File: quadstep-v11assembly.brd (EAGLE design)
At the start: 57.8 x 122.4 mm, 115 parts, among them U1 A4983, U3 A4983, U4 A4983, U5 A4983, X1 MSTBA4, X2 MSTBA4, X3 MSTBA4, X4 MSTBA4

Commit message: Clean-up of the layout.
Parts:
- removed C10, C11, C18, C19, C21, C22, C23, C27, C28, C29, C3, C4, C46, C47, C49: 0.1uF, SparkFun:0402-CAP
- removed C20, C6, C8: 0.22uF, SparkFun:0402-CAP
- removed JP1, JP14, JP15, JP2, JP7, JP8: (no value), SparkFun:SCREWTERMINAL-3.5MM-2_LOCK
- removed LED1, LED3, LED4: green, SparkFun:LED-0603
- removed R1, R18, R19, R2, R4, R5: 0.22, SparkFun:0805
- removed R17, R24, R3: Trimpot, SparkFun:TRIMPOT-3MM
- removed R20, R6, R66: 20k, SparkFun:0402-RES
- removed R21, R28, R7: 330, SparkFun:0402-RES
- removed R31, R32, R33, R37, R38, R39, R40, R45, R46, R47, R48, R8: 10k, SparkFun:0402-RES
- removed SJ14, SJ15, SJ16, SJ17, SJ2, SJ3, SJ4, SJ5, SJ6, SJ7, SJ8, SJ9: SOLDERJUMPERNO, SparkFun:SJ_2S-NO
- removed TP1, TP2, TP3: TEST-POINT3X5, SparkFun:PAD.03X.05
- removed U1, U4, U5: A4983, SparkFun:QFN-28-5MM
- removed X1, X2, X4: MSTBA4, con-phoenix-508:MSTBA4
- moved SJ26 69.1 mm to (23.2, 23.3), turned to 90 degrees
- moved C32 68.8 mm to (21.4, 20.7), turned to 90 degrees
- moved R61 65.0 mm to (30.4, 26.7), turned to 90 degrees
- moved C30 60.3 mm to (27.7, 19.1), turned to 90 degrees
- moved SJ1 56.1 mm to (40.8, 26.5), turned to 90 degrees
- moved R62 54.6 mm to (33.6, 19.6), turned to 90 degrees
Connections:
- removed net DIR1: U1.P$19
- removed net DIR2: U5.P$19
- removed net DIR4: U4.P$19
- removed net MS11: R32.2, SJ4.2, U1.P$9
- removed net MS12: R38.2, SJ8.2, U5.P$9
- removed net MS14: R47.2, SJ16.2, U4.P$9
- removed net MS21: R31.2, SJ3.2, U1.P$10
- removed net MS22: R39.2, SJ7.2, U5.P$10
- removed net MS24: R46.2, SJ15.2, U4.P$10
- removed net MS31: R8.2, SJ2.2, U1.P$11
- removed net MS32: R40.2, SJ6.2, U5.P$11
- removed net MS34: R45.2, SJ14.2, U4.P$11
- removed net N$10: C47.1, U1.P$6
- removed net N$11: C8.1, U1.P$8
- removed net N$12: R66.1, U1.P$13
- removed net N$13: C46.1, U1.P$4
- removed net N$14: R3.2, TP1.P$1, U1.P$17
- removed net N$15: C46.2, U1.P$5
- removed net N$17: LED1.C, R7.1
- removed net N$2: JP1.1, U1.P$21
- removed net N$3: JP1.2, U1.P$24
- removed net N$32: R18.2, U4.P$23
- removed net N$33: R19.2, U4.P$27
- removed net N$34: C19.1, U4.P$6
- removed net N$35: C20.1, U4.P$8
- removed net N$36: R20.1, U4.P$13
- removed net N$37: R17.2, TP3.P$1, U4.P$17
- removed net N$38: C18.1, U4.P$4
- removed net N$39: C18.2, U4.P$5
- removed net N$40: LED3.C, R21.1
- removed net N$41: JP7.1, U4.P$21
- removed net N$42: JP7.2, U4.P$24
- removed net N$43: JP8.1, U4.P$26
- removed net N$44: JP8.2, U4.P$1
- removed net N$45: R1.2, U5.P$23
- removed net N$46: R2.2, U5.P$27
- removed net N$47: C4.1, U5.P$6
- removed net N$48: C6.1, U5.P$8
- removed net N$49: R6.1, U5.P$13
- removed net N$50: R24.2, TP2.P$1, U5.P$17
- removed net N$51: C3.1, U5.P$4
- removed net N$52: C3.2, U5.P$5
- removed net N$53: LED4.C, R28.1
- removed net N$54: JP14.1, U5.P$21
- removed net N$55: JP14.2, U5.P$24
- removed net N$56: JP15.1, U5.P$26
- removed net N$57: JP15.2, U5.P$1
- removed net N$6: JP2.1, U1.P$26
- removed net N$7: JP2.2, U1.P$1
- removed net N$8: R4.2, U1.P$23
- removed net N$9: R5.2, U1.P$27
- removed net RST1: R33.2, SJ5.2, U1.P$12
- removed net RST2: R37.2, SJ9.2, U5.P$12
- removed net RST4: R48.2, SJ17.2, U4.P$12
- removed net STP1: LED1.A, U1.P$16
- removed net STP2: LED4.A, U5.P$16
- removed net STP4: LED3.A, U4.P$16
- net EN: no longer U1.P$2, U4.P$2, U5.P$2
- net GND: no longer C10.2, C11.2, C20.2, C21.2, C22.2, C23.2, C27.2, C28.2, C29.2, C49.2, C6.2, C8.2, R1.1, R17.1, R18.1, R19.1, R2.1, R20.2, R21.2, R24.1, R28.2, R3.1, R4.1, R5.1, R6.2, R66.2, R7.2, SJ14.1, SJ15.1, SJ16.1, SJ17.1, SJ2.1, SJ3.1, SJ4.1, SJ5.1, SJ6.1, SJ7.1, SJ8.1, SJ9.1, U1.P$18, U1.P$29, U1.P$3, U4.P$18, U4.P$29, U4.P$3, U5.P$18, U5.P$29, U5.P$3
- net SLP: no longer U1.P$14, U4.P$14
- net VCC: no longer C10.1, C11.1, C19.2, C22.1, C23.1, C28.1, C29.1, C4.2, C47.2, U1.P$22, U1.P$28, U4.P$22, U4.P$28, U5.P$22, U5.P$28
- net VOUT: no longer C21.1, C27.1, C49.1, R17.3, R24.3, R3.3, R31.1, R32.1, R33.1, R37.1, R38.1, R39.1, R40.1, R45.1, R46.1, R47.1, R48.1, R8.1, U1.P$15, U4.P$15, U5.P$15
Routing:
- net VOUT: track 221.1 -> 20.7 mm, vias 28 -> 2
- net VCC: track 152.4 -> 21.8 mm, vias 17 -> 5
- net N$37: track 45.6 -> 0.00 mm, vias 1 -> 0
- net GND: track 61.9 -> 26.4 mm, vias 89 -> 15
- net N$14: track 31.2 -> 0.00 mm, vias 2 -> 0
- net N$50: track 23.7 -> 0.00 mm, vias 3 -> 0
- net STP2: track 17.3 -> 0.00 mm
- net N$57: track 15.0 -> 0.00 mm
- net N$7: track 14.9 -> 0.00 mm
- net N$44: track 14.9 -> 0.00 mm
- net N$54: track 14.9 -> 0.00 mm
- net N$2: track 14.7 -> 0.00 mm
- net N$41: track 14.2 -> 0.00 mm
- net N$56: track 12.3 -> 0.00 mm
- net N$42: track 12.2 -> 0.00 mm
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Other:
- board size 57.8 x 122.4 mm -> 50 x 50 mm
- board text removed: "1"
- board text removed: "2"
- board text removed: "3"
- board text removed: "4"
- board text removed: "Bus"
- board text removed: "DIR"
- board text removed: "Enable"
- board text removed: "STP"

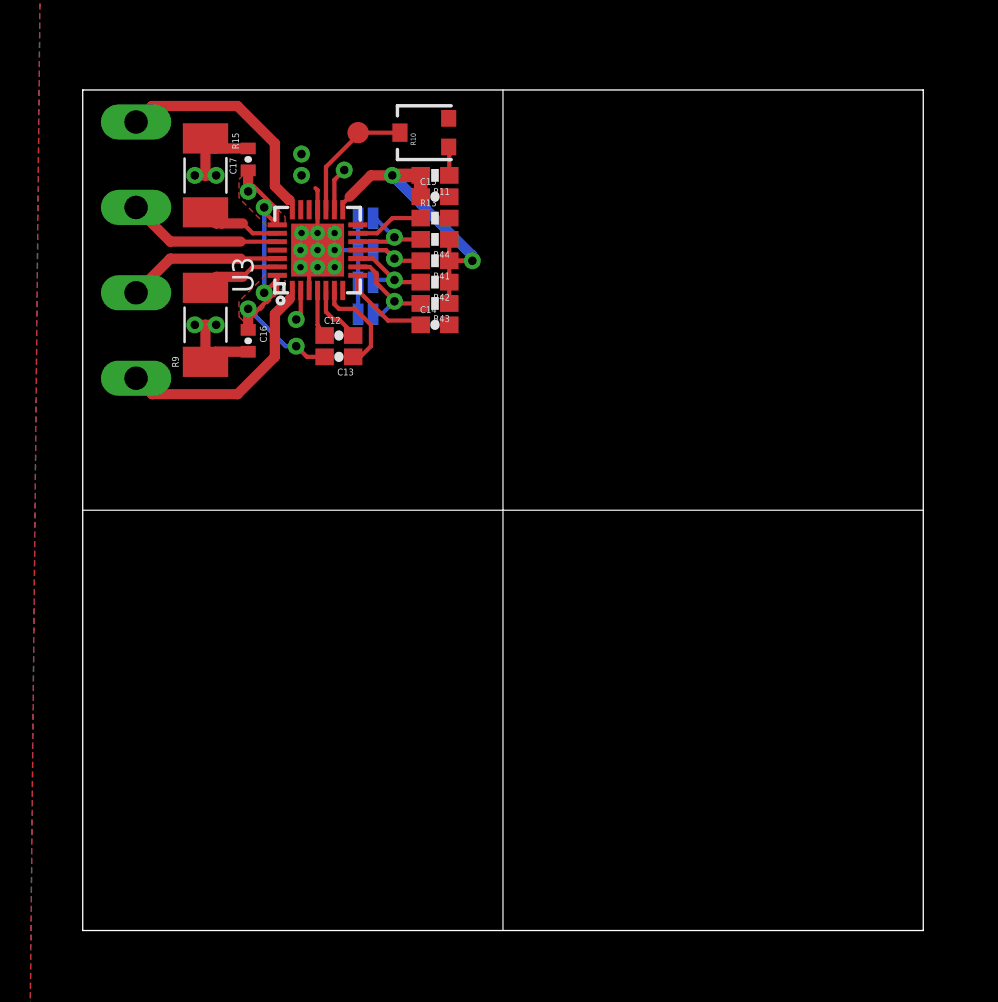
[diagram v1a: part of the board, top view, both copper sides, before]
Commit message: Layout copied to the other three quadrants.
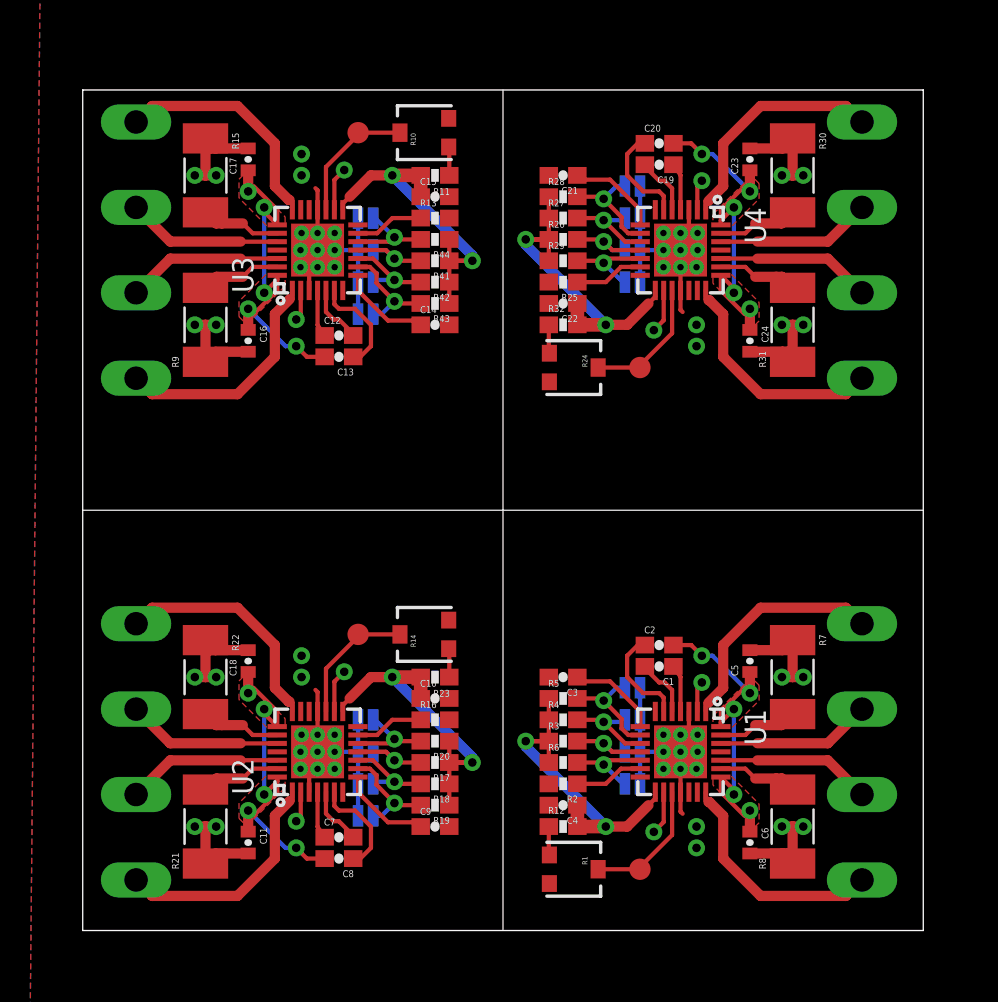
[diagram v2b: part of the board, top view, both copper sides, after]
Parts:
- added C1, C10, C19, C2, C20, C22, C4, C7, C8: 0.1uF, SparkFun:0603-CAP
- added C11, C18, C23, C24, C5, C6: 0.1uF, SparkFun:0402-CAP
- added C21, C3, C9: 0.22uF, SparkFun:0603-CAP
- added R1, R14, R24: Trimpot, SparkFun:TRIMPOT-3MM
- added R12, R17, R18, R19, R20, R23, R26, R27, R28, R29, R3, R32, R4, R5, R6: 10k, SparkFun:0603-RES
- added R16, R2, R25: 20k, SparkFun:0603-RES
- added R21, R22, R30, R31, R7, R8: .11, SparkFun:R2010
- added SJ14, SJ15, SJ16, SJ17, SJ2, SJ3, SJ4, SJ5, SJ6, SJ7, SJ8, SJ9: SOLDERJUMPERNO, SparkFun:SJ_2S-NO
- added TP1, TP2, TP3: TEST-POINT3X5, SparkFun:PAD.03X.05
- added U1, U2, U4: A4983, SparkFun:QFN-28-5MM
- added X1, X2, X4: MSTBA4, con-phoenix-508:MSTBA4
- moved X3 61.1 mm to (51.4, -39.4), turned to 270 degrees
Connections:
- net DIR3 renamed DIR-1
- net MS13 renamed MS1-1
- net MS23 renamed MS2-1
- net MS33 renamed MS3-1
- net RST3 renamed RST-1
- net STP3 renamed STP-1
- new net DIR-2: U2.P$19
- new net DIR-3: U1.P$19
- new net DIR-4: U4.P$19
- new net MS1-2: R19.2, SJ8.2, U2.P$9
- new net MS1-3: R5.2, SJ4.2, U1.P$9
- new net MS1-4: R28.2, SJ16.2, U4.P$9
- new net MS2-2: R18.2, SJ7.2, U2.P$10
- new net MS2-3: R4.2, SJ3.2, U1.P$10
- new net MS2-4: R27.2, SJ15.2, U4.P$10
- new net MS3-2: R17.2, SJ6.2, U2.P$11
- new net MS3-3: R3.2, SJ2.2, U1.P$11
- new net MS3-4: R26.2, SJ14.2, U4.P$11
- new net N$10: U1.P$24, X3.3
- new net N$11: U1.P$26, X3.2
- new net N$12: U1.P$1, X3.1
- new net N$13: U1.P$21, X3.4
- new net N$14: R7.2, U1.P$27
- new net N$15: R8.2, U1.P$23
- new net N$16: R1.1, R12.1
- new net N$17: C8.1, U2.P$6
- new net N$18: C9.1, U2.P$8
- new net N$2: C2.1, U1.P$6
- new net N$24: R16.1, U2.P$13
- new net N$26: R14.2, TP2.P$1, U2.P$17
- new net N$3: C3.1, U1.P$8
- new net N$32: C7.1, U2.P$4
- new net N$33: C7.2, U2.P$5
- new net N$34: U2.P$24, X2.3
- new net N$35: U2.P$26, X2.2
- new net N$36: U2.P$1, X2.1
- new net N$37: U2.P$21, X2.4
- new net N$38: R21.2, U2.P$27
- new net N$39: R22.2, U2.P$23
- new net N$40: R14.1, R23.1
- new net N$41: C20.1, U4.P$6
- new net N$42: C21.1, U4.P$8
- new net N$43: R25.1, U4.P$13
- new net N$44: R24.2, TP3.P$1, U4.P$17
- new net N$45: C19.1, U4.P$4
- new net N$46: C19.2, U4.P$5
- new net N$47: U4.P$24, X4.3
- new net N$48: U4.P$26, X4.2
- new net N$49: U4.P$1, X4.1
- new net N$50: U4.P$21, X4.4
- new net N$51: R30.2, U4.P$27
- new net N$52: R31.2, U4.P$23
- new net N$53: R24.1, R32.1
- new net N$6: R2.1, U1.P$13
- new net N$7: R1.2, TP1.P$1, U1.P$17
- new net N$8: C1.1, U1.P$4
- new net N$9: C1.2, U1.P$5
- new net RST-2: R20.2, SJ9.2, U2.P$12
- new net RST-3: R6.2, SJ5.2, U1.P$12
- new net RST-4: R29.2, SJ17.2, U4.P$12
- new net STP-2: U2.P$16
- new net STP-3: U1.P$16
- new net STP-4: U4.P$16
- net EN: now also U1.P$2, U2.P$2, U4.P$2
- net GND: now also C10.2, C11.2, C18.2, C21.2, C22.2, C23.2, C24.2, C3.2, C4.2, C5.2, C6.2, C9.2, R1.3, R14.3, R16.2, R2.2, R21.1, R22.1, R24.3, R25.2, R30.1, R31.1, R7.1, R8.1, SJ14.1, SJ15.1, SJ16.1, SJ17.1, SJ2.1, SJ3.1, SJ4.1, SJ5.1, SJ6.1, SJ7.1, SJ8.1, SJ9.1, U1.P$18, U1.P$29, U1.P$3, U2.P$18, U2.P$29, U2.P$3, U4.P$18, U4.P$29, U4.P$3
- net N$28: now also X1.4; no longer X3.4
- net N$29: now also X1.3; no longer X3.3
- net N$30: now also X1.2; no longer X3.2
- net N$31: now also X1.1; no longer X3.1
- net SLP: now also U1.P$14, U2.P$14, U4.P$14
- net VCC: now also C11.1, C18.1, C2.2, C20.2, C23.1, C24.1, C5.1, C6.1, C8.2, U1.P$22, U1.P$28, U2.P$22, U2.P$28, U4.P$22, U4.P$28
- net VOUT: now also C10.1, C22.1, C4.1, R12.2, R17.1, R18.1, R19.1, R20.1, R23.2, R26.1, R27.1, R28.1, R29.1, R3.1, R32.2, R4.1, R5.1, R6.1, U1.P$15, U2.P$15, U4.P$15
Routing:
- net GND: track 26.4 -> 105.6 mm, vias 15 -> 60
- net VCC: track 21.8 -> 87.3 mm, vias 5 -> 20
- net VOUT: track 20.7 -> 82.8 mm, vias 2 -> 8
- net N$50: track 0.00 -> 14.0 mm
- net N$37: track 0.00 -> 14.0 mm
- net N$13: track 0.00 -> 14.0 mm
- net N$49: track 0.00 -> 13.9 mm
- net N$36: track 0.00 -> 13.9 mm
- net N$12: track 0.00 -> 13.9 mm
- net N$35: track 0.00 -> 9.24 mm
- net N$34: track 0.00 -> 9.24 mm
- net N$48: track 0.00 -> 9.24 mm
- net N$11: track 0.00 -> 9.24 mm
- net N$47: track 0.00 -> 9.24 mm
- net N$10: track 0.00 -> 9.24 mm
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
